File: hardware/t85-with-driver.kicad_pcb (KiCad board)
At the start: 2 copper layers, 49.5 x 22.9 mm, 11 parts, among them CN1 .1u, J1 AVRISP6, P1 Ethertiny, P3 EXTCON, T1 S553-5999-52, U1 ATTINY85, U2 RS485-ISL3170

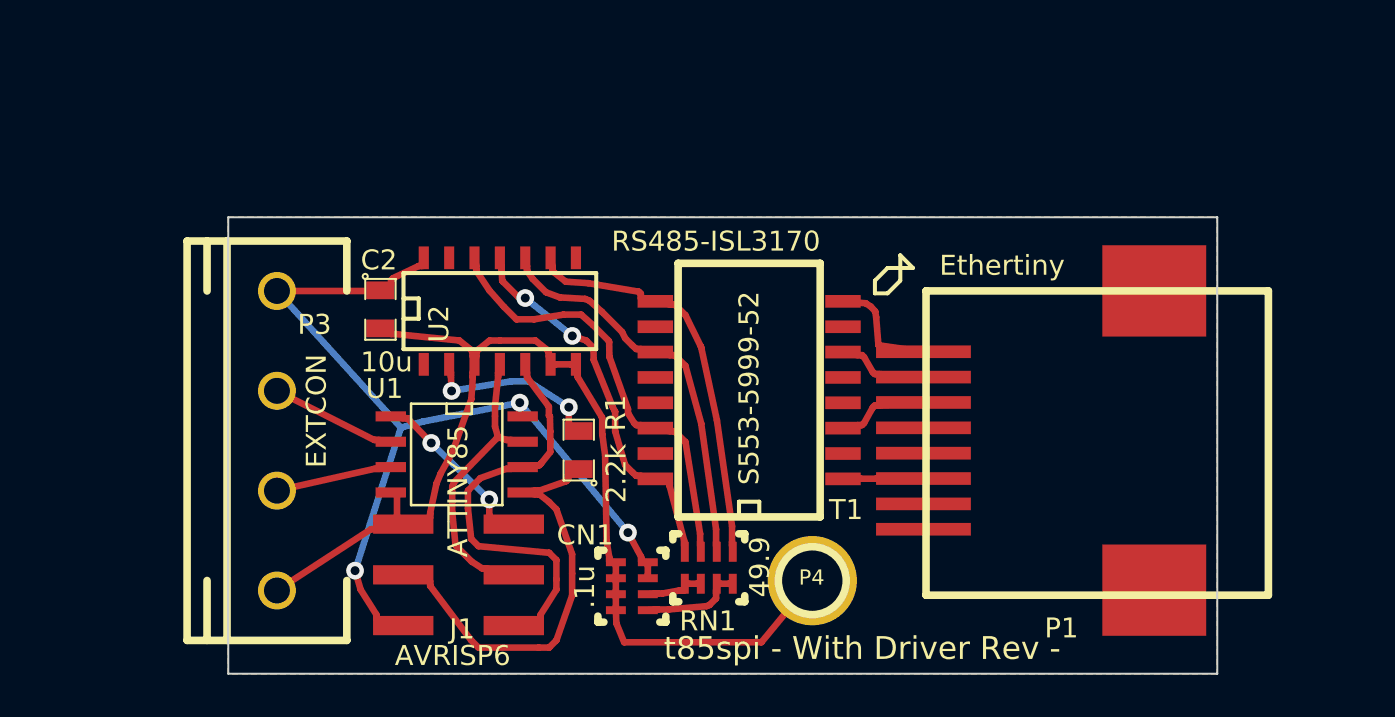
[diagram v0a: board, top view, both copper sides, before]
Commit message: add documentation + warnings
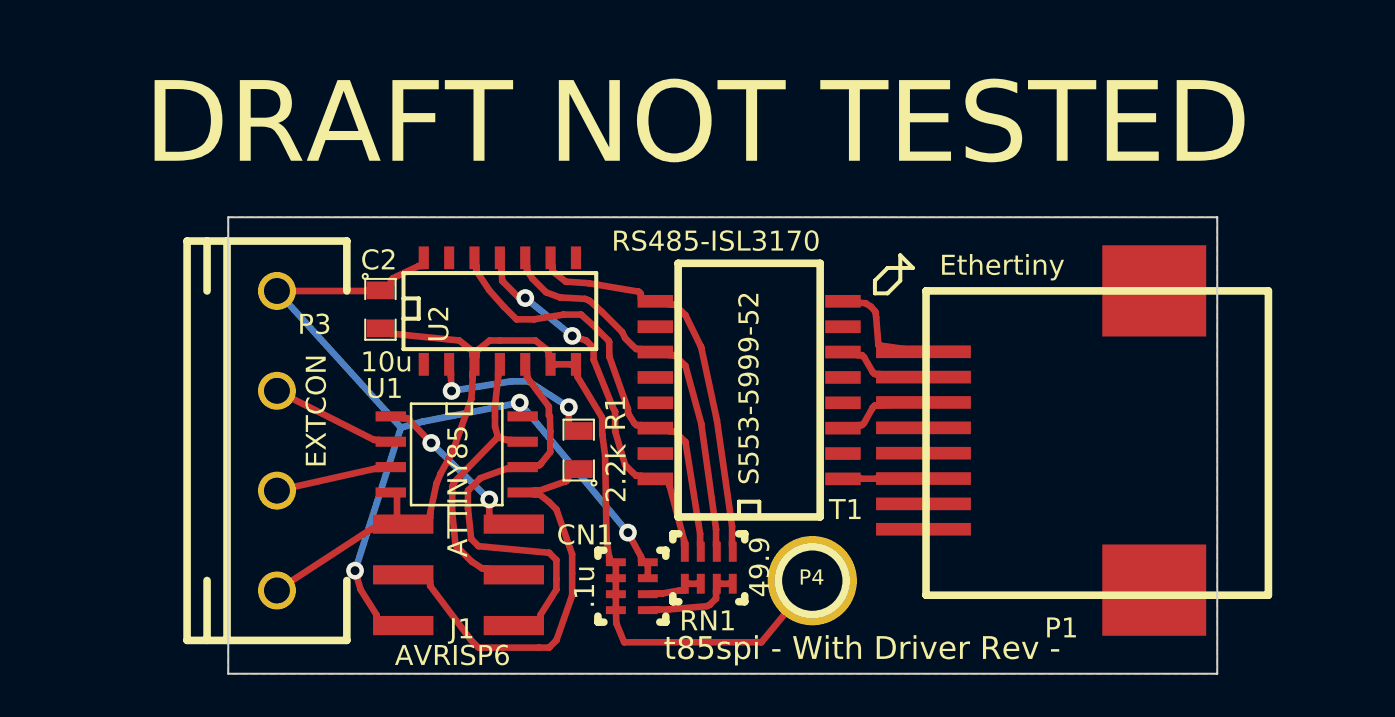
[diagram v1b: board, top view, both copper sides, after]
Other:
- board text added: "DRAFT NOT TESTED"
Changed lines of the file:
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@@
     (links 43)
     (no_connects 0)
-    (area 73.609999 50.749999 123.240001 73.710001)
+    (area 71.103099 50.717919 126.244601 73.710001)
     (thickness 1.6)
-    (drawings 19)
+    (drawings 20)
     (tracks 384)
     (zones 0)
@@
     )
   )
+  (gr_text "DRAFT NOT TESTED" (at 97.155 46.101) (layer F.SilkS)
+    (effects (font (size 4.04 4.04) (thickness 0.3)))
+  )
   (gr_text VCC (at 79.375 53.34) (layer B.SilkS)
